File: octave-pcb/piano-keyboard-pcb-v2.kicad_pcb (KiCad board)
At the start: 2 copper layers, 160.8 x 35.6 mm, 29 parts, among them J1 Conn_01x05_Male, J2 Conn_01x05_Female, SW1 SW_SPDT, SW10 SW_SPDT, SW11 SW_SPDT, SW12 SW_SPDT, SW2 SW_SPDT, SW3 SW_SPDT, SW4 SW_SPDT, SW5 SW_SPDT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

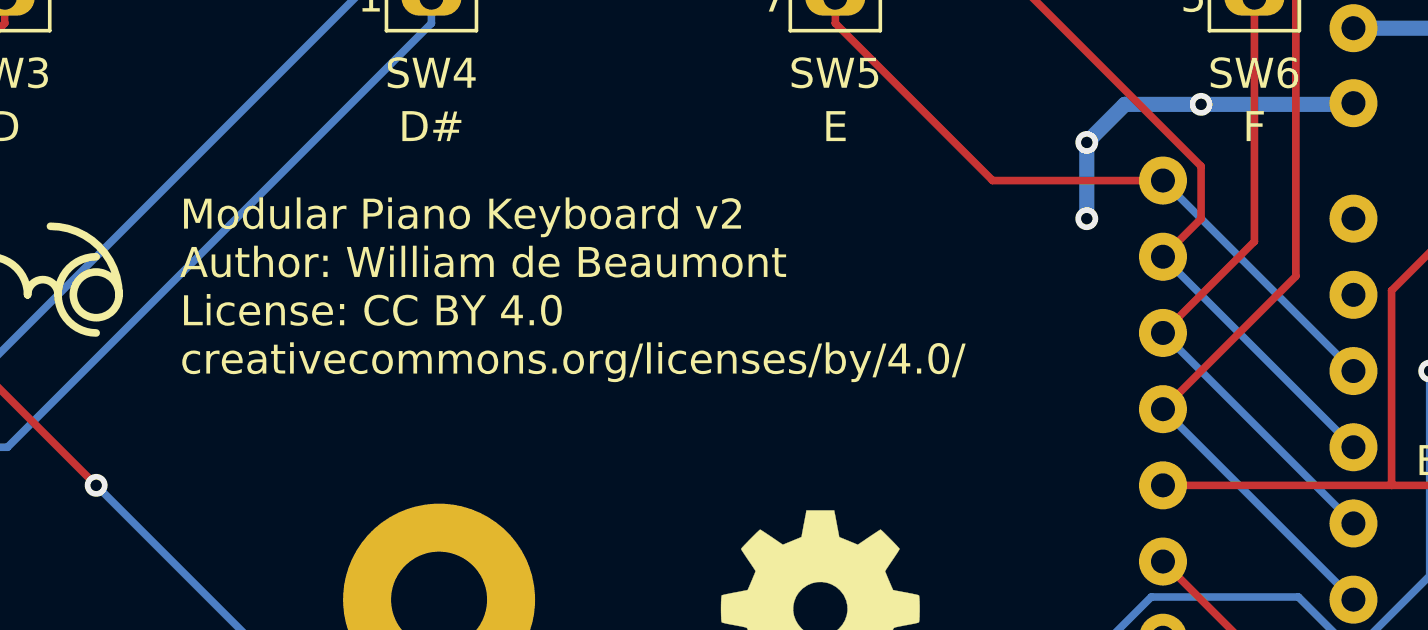
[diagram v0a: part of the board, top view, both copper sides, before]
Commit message: add github link to octave pcb silkscreen; adjust placement of "J2" silkscreen so it doesn't get cut off
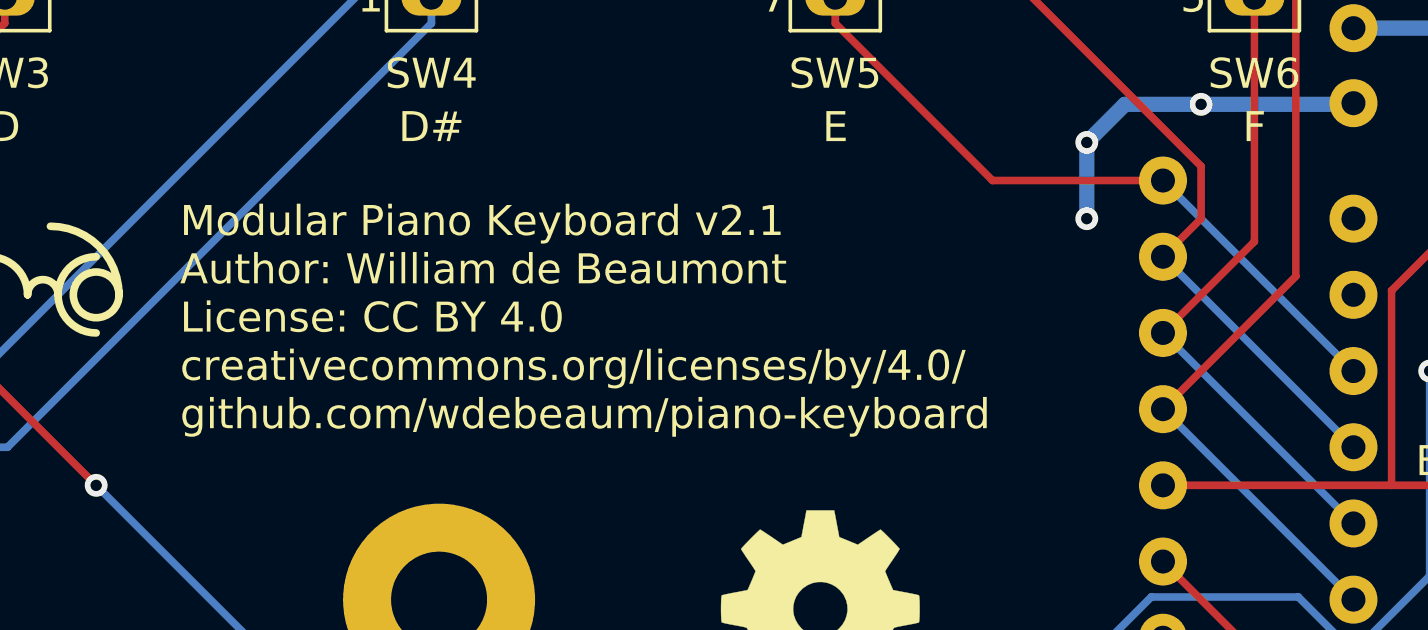
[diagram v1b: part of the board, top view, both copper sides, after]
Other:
- board text added: "Modular Piano Keyboard v2.1 Author: William de Beaumont License: CC BY 4.0 creativecommons.org/licenses/by/4.0/ github.com/wdebeaum/piano-keyboard"
- board text removed: "Modular Piano Keyboard v2 Author: William de Beaumont License: CC BY 4.0 creativecommons.org/licenses/by/4.0/"
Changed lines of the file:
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@@
     (title "Modular Piano Keyboard")
     (date 2020-03-05)
-    (rev v2)
+    (rev v2.1)
     (comment 2 creativecommons.org/licenses/by/4.0/)
     (comment 3 "License: CC BY 4.0")
@@
     (descr "Through hole angled socket strip, 1x05, 2.54mm pitch, 8.51mm socket length, single row (from Kicad 4.0.7), script generated")
     (tags "Through hole angled socket strip THT 1x05 2.54mm single row")
-    (fp_text reference J2 (at -4.38 2.77 180) (layer B.SilkS)
+    (fp_text reference J2 (at -3.81 2.794 180) (layer B.SilkS)
       (effects (font (size 1 1) (thickness 0.15)) (justify mirror))
     )
@@
     (effects (font (size 1 1) (thickness 0.15)) (justify left))
   )
-  (gr_text "Modular Piano Keyboard v2\nAuthor: William de Beaumont\nLicense: CC BY 4.0\ncreativecommons.org/licenses/by/4.0/" (at 66.294 41.656) (layer F.SilkS)
+  (gr_text "Modular Piano Keyboard v2.1\nAuthor: William de Beaumont\nLicense: CC BY 4.0\ncreativecommons.org/licenses/by/4.0/\ngithub.com/wdebeaum/piano-keyboard" (at 66.294 42.672) (layer F.SilkS)
     (effects (font (size 1 1) (thickness 0.15)) (justify left))
   )
